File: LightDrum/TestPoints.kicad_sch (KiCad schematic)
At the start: 9 parts

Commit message: Preliminary schematic lock - Starting PCB layout
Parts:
- TP1101, TP1102, TPA1301, TPA1302: SupplierPN (none) -> 36-5002-ND
- TPA1101, TPA1103, TPA1104, TPA1201: SupplierPN (none) -> 36-5000-ND
- TPA1102: SupplierPN (none) -> 36-5001-ND
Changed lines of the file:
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@@
   (title_block
     (title "LightDrum")
-    (rev "REV10")
+    (rev "REV11")
     (company "Daxxn Industries")
   )
@@
       (effects (font (size 1.27 1.27)) hide)
     )
+    (property "SupplierPN" "36-5002-ND" (at 33.02 25.4 0)
+      (effects (font (size 1.27 1.27)) hide)
+    )
     (pin "1")
     (pin "2")
@@
       (effects (font (size 1.27 1.27)) hide)
     )
+    (property "SupplierPN" "36-5000-ND" (at 58.42 25.4 0)
+      (effects (font (size 1.27 1.27)) hide)
+    )
     (pin "1")
     (instances
@@
       (effects (font (size 1.27 1.27)) hide)
     )
+    (property "SupplierPN" "36-5002-ND" (at 33.02 33.02 0)
+      (effects (font (size 1.27 1.27)) hide)
+    )
     (pin "1")
     (pin "2")
@@
       (effects (font (size 1.27 1.27)) hide)
     )
+    (property "SupplierPN" "36-5002-ND" (at 27.94 49.53 0)
+      (effects (font (size 1.27 1.27)) hide)
+    )
     (pin "1")
     (instances
@@
       (effects (font (size 1.27 1.27)) hide)
     )
+    (property "SupplierPN" "36-5000-ND" (at 58.42 40.64 0)
+      (effects (font (size 1.27 1.27)) hide)
+    )
     (pin "1")
     (instances
@@
       (effects (font (size 1.27 1.27)) hide)
     )
+    (property "SupplierPN" "36-5002-ND" (at 27.94 40.64 0)
+      (effects (font (size 1.27 1.27)) hide)
+    )
     (pin "1")
     (instances
@@
       (effects (font (size 1.27 1.27)) hide)
     )
+    (property "SupplierPN" "36-5001-ND" (at 58.42 54.61 0)
+      (effects (font (size 1.27 1.27)) hide)
+    )
     (pin "1")
     (instances
@@
       (effects (font (size 1.27 1.27)) hide)
     )
+    (property "SupplierPN" "36-5000-ND" (at 58.42 33.02 0)
+      (effects (font (size 1.27 1.27)) hide)
+    )
     (pin "1")
     (instances
@@
       (effects (font (size 1.27 1.27)) hide)
     )
+    (property "SupplierPN" "36-5000-ND" (at 58.42 48.26 0)
+      (effects (font (size 1.27 1.27)) hide)
+    )

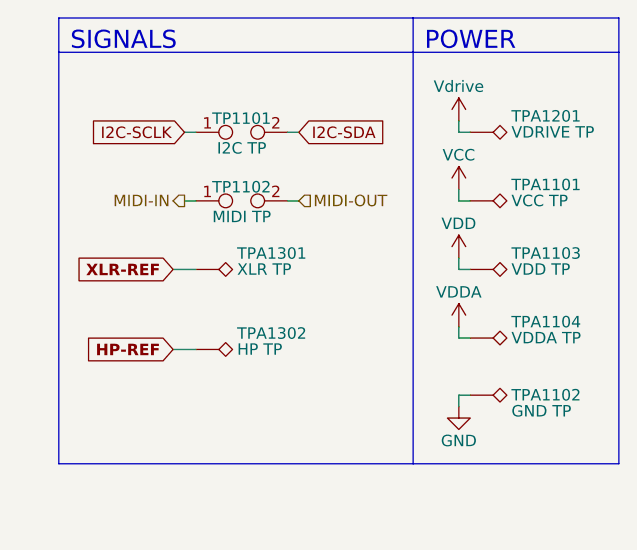
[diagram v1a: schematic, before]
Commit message: Component placement complete
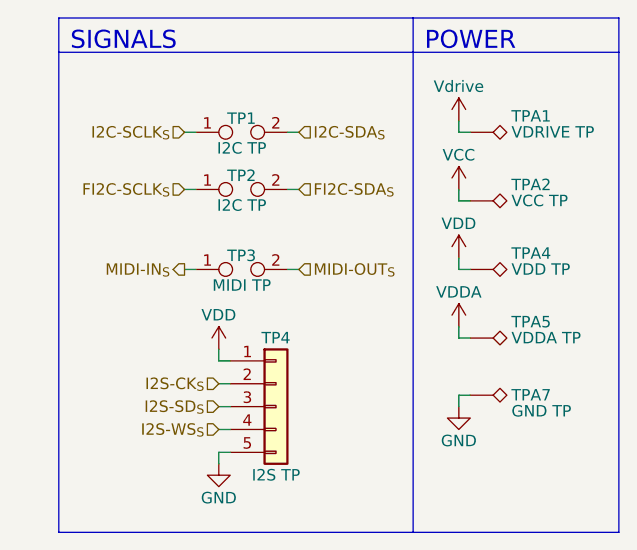
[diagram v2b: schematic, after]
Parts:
- removed TPA1301: XLR TP, TestPoint:TestPoint_Pad_D1.5mm, symbol Connector:TestPoint_Alt
- removed TPA1302: HP TP, TestPoint:TestPoint_Pad_D1.5mm, symbol Connector:TestPoint_Alt
- added TP2: I2C TP, Connector_PinHeader_1.27mm:PinHeader_1x02_P1.27mm_Vertical, symbol Connector:TestPoint_2Pole
- added TP4: I2S TP, Connector_PinHeader_1.27mm:PinHeader_1x05_P1.27mm_Vertical, symbol Connector_Generic:Conn_01x05
- TP1: renamed from TP1101; footprint Connector_PinHeader_2.54mm:PinHeader_1x02_P2.54mm_Vertical -> Connector_PinHeader_1.27mm:PinHeader_1x02_P1.27mm_Vertical
- TP3: renamed from TP1102; footprint Connector_PinHeader_2.54mm:PinHeader_1x02_P2.54mm_Vertical -> Connector_PinHeader_1.27mm:PinHeader_1x02_P1.27mm_Vertical
- renumbered TPA1201 to TPA1, TPA1101 to TPA2, TPA1103 to TPA4, TPA1104 to TPA5, TPA1102 to TPA7
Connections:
- net GND: now also TP4.5 (Pin_5)
- net VDD: now also TP4.1 (Pin_1)
- net I2C-SCLK renamed I2C-SCLK_{S}
- net I2C-SDA renamed I2C-SDA_{S}
- net MIDI-IN renamed MIDI-IN_{S}
- net MIDI-OUT renamed MIDI-OUT_{S}
- new net FI2C-SCLK_{S}: TP2.1
- new net FI2C-SDA_{S}: TP2.2
- new net I2S-CK_{S}: TP4.2 (Pin_2)
- new net I2S-SD_{S}: TP4.3 (Pin_3)
- new net I2S-WS_{S}: TP4.4 (Pin_4)
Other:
- moved on the sheet: TP3

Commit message: Replace DSub with much better ECU conn
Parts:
- TP1, TP2, TP3: footprint Connector_PinHeader_1.27mm:PinHeader_1x02_P1.27mm_Vertical -> Connector_PinHeader_2.54mm:PinHeader_1x02_P2.54mm_Vertical
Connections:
- net VDDA renamed VAA
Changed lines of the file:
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@@
       (effects (font (size 1.27 1.27)))
     )
-    (property "Footprint" "Connector_PinHeader_1.27mm:PinHeader_1x02_P1.27mm_Vertical" (at 33.02 25.4 0)
+    (property "Footprint" "Connector_PinHeader_2.54mm:PinHeader_1x02_P2.54mm_Vertical" (at 33.02 25.4 0)
       (effects (font (size 1.27 1.27)) hide)
     )
@@
       (effects (font (size 1.27 1.27)))
     )
-    (property "Footprint" "Connector_PinHeader_1.27mm:PinHeader_1x02_P1.27mm_Vertical" (at 33.02 31.75 0)
+    (property "Footprint" "Connector_PinHeader_2.54mm:PinHeader_1x02_P2.54mm_Vertical" (at 33.02 31.75 0)
       (effects (font (size 1.27 1.27)) hide)
     )
@@
       (effects (font (size 1.27 1.27)))
     )
-    (property "Footprint" "Connector_PinHeader_1.27mm:PinHeader_1x02_P1.27mm_Vertical" (at 33.02 40.64 0)
+    (property "Footprint" "Connector_PinHeader_2.54mm:PinHeader_1x02_P2.54mm_Vertical" (at 33.02 40.64 0)
       (effects (font (size 1.27 1.27)) hide)
     )
@@
     )
   )
+  (symbol (lib_id "power:VAA") (at 57.15 46.99 0) (unit 1)
+    (in_bom yes) (on_board yes) (dnp no)
+    (property "Reference" "#PWR040" (at 57.15 50.8 0)
+      (effects (font (size 1.27 1.27)) hide)
+    )
+    (property "Value" "VAA" (at 57.15 43.18 0)
+      (effects (font (size 1.27 1.27)))
+    )
+    (property "Footprint" "" (at 57.15 46.99 0)
+      (effects (font (size 1.27 1.27)) hide)
+    )
+    (property "Datasheet" "" (at 57.15 46.99 0)
+      (effects (font (size 1.27 1.27)) hide)
+    )
+    (pin "1")
+    (instances
+      (project "LightDrum"
+        (path "/7f137461-fd46-4a4c-8db7-555d487fb3ca/1cf17c4e-5921-408b-a9f8-9e373eae7d69"
+          (reference "#PWR040") (unit 1)
+        )
+        (path "/7f137461-fd46-4a4c-8db7-555d487fb3ca/47dd7232-a18b-43ab-b8d2-1101988d95b2"
+          (reference "#PWR0108") (unit 1)
+        )
+      )
+    )
+  )
   (symbol (lib_id "power:VCC") (at 57.15 31.75 0) (unit 1)
     (in_bom yes) (on_board yes) (dnp no)
@@
         )
       )
-    )
-  )
-  (symbol (lib_id "power:VDDA") (at 57.15 46.99 0) (unit 1)
-    (in_bom yes) (on_board yes) (dnp no)
-    (property "Reference" "#PWR0108" (at 57.15 50.8 0)
-      (effects (font (size 1.27 1.27)) hide)
-    )
-    (property "Value" "VDDA" (at 57.15 43.18 0)
-      (effects (font (size 1.27 1.27)))
-    )
-    (property "Footprint" "" (at 57.15 46.99 0)
-      (effects (font (size 1.27 1.27)) hide)
-    )
-    (property "Datasheet" "" (at 57.15 46.99 0)
-      (effects (font (size 1.27 1.27)) hide)
-    )
-    (pin "1")
-    (instances
-      (project "LightDrum"
-        (path "/7f137461-fd46-4a4c-8db7-555d487fb3ca/47dd7232-a18b-43ab-b8d2-1101988d95b2"
-          (reference "#PWR0108") (unit 1)
-        )
-      )

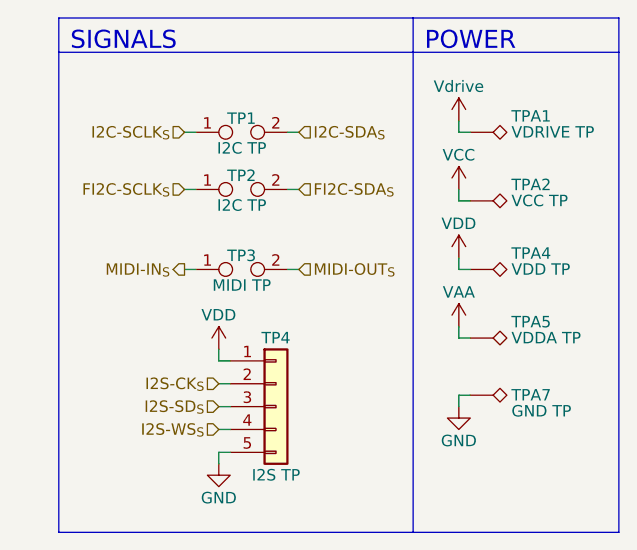
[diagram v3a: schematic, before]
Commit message: Organize old files and generate interface gerbers
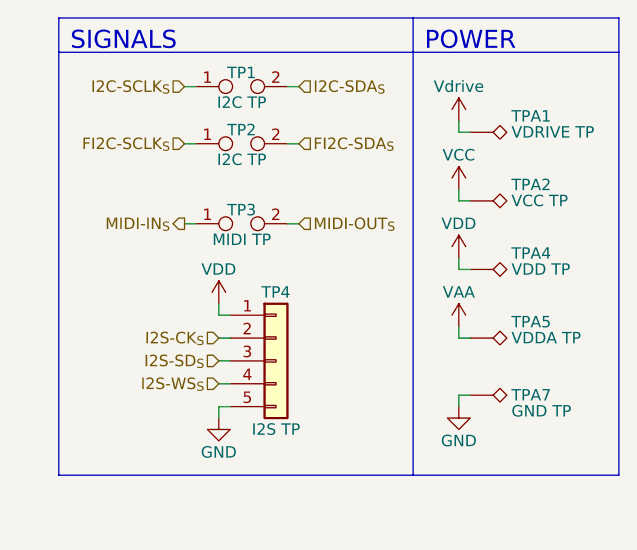
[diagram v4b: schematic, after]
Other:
- moved on the sheet: TP1, TP2, TP3, TP4
